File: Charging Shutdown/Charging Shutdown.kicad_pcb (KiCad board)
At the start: 2 copper layers, 45.6 x 49.9 mm, 13 parts, among them J2 776280-1, K1 PR2212V4001A, K3 PR2212V4001A, Q1 2N2222, Q3 2N2222

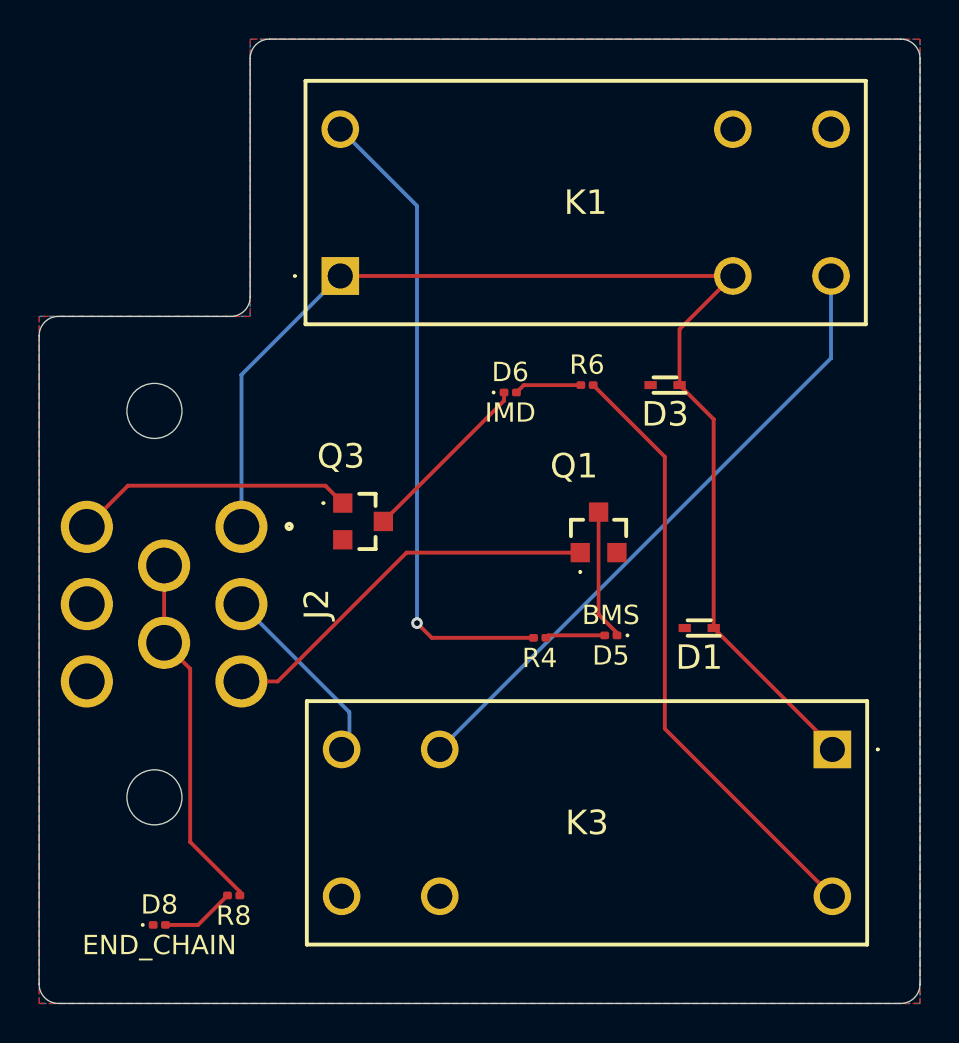
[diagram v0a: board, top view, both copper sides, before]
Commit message: Footprint fixes for Charging Shutdown + Gerbers
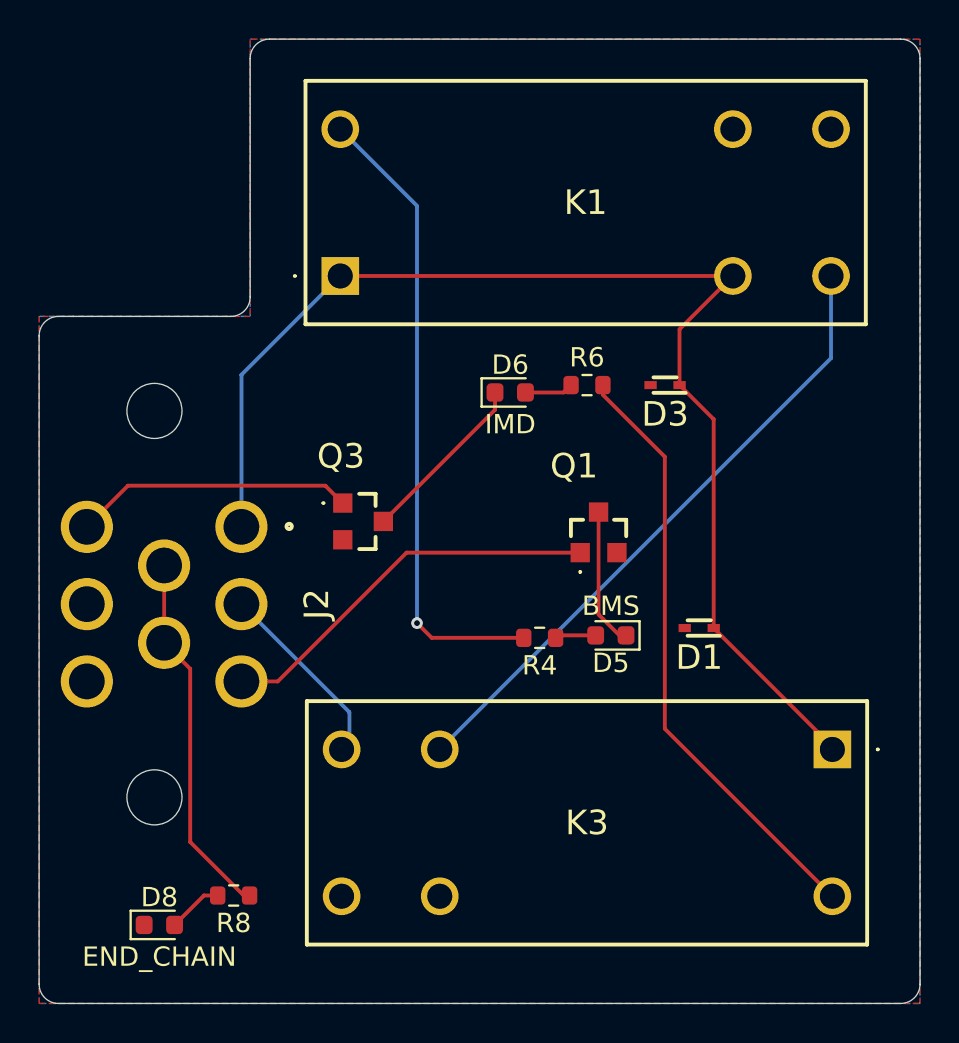
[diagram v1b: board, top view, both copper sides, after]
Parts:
- D5, D6, D8: footprint LED_SMD:LED_0201_0603Metric -> LED_SMD:LED_0603_1608Metric
- R4, R6, R8: footprint Resistor_SMD:R_0201_0603Metric -> Resistor_SMD:R_0603_1608Metric
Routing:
- net Net-(D8-A): track 3.84 -> 2.86 mm
- net Net-(D6-A): track 3.49 -> 2.52 mm
- net Net-(D5-A): track 3.10 -> 2.12 mm
- net Net-(K1-COIL_2): track 33.6 -> 33.1 mm
